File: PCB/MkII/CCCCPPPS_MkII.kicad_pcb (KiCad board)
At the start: 2 copper layers, 58 x 20 mm, 30 parts, among them J1 PROG_HEADER, J2 USB_C, J3 CONN_OUT, J4 CONN_IN, Q1 AO3400A, U2 CH32V003AxMx, U3 AP2112K-3.3

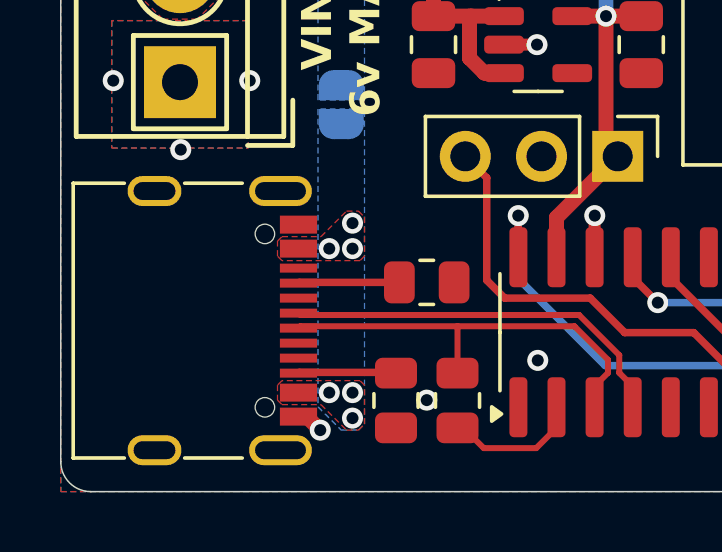
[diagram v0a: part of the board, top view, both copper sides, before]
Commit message: Fixed MkII USB and Polarity issues. MkIIB
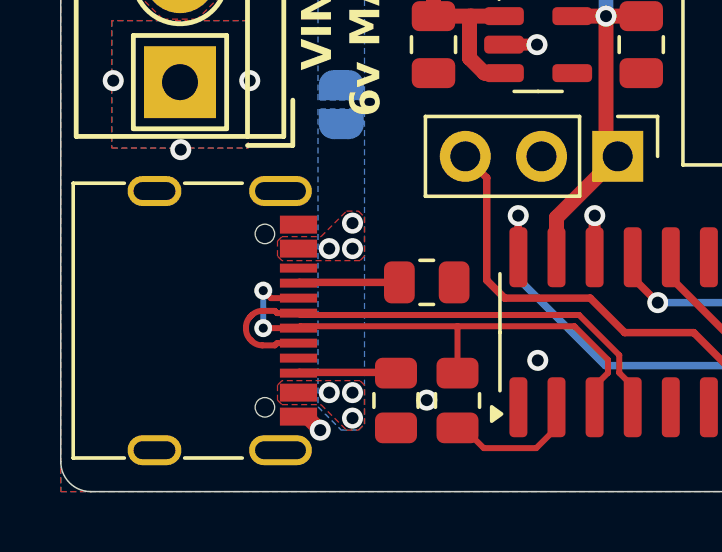
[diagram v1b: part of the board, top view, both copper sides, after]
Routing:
- net /USB_DP: track 13.2 -> 17.4 mm
- net /USB_DN: track 14.1 -> 17.8 mm, vias 0 -> 2
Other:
- board text added: "+"
- board text added: "-"
- board text added: "2024 MkIIB ADBeta Bogdan Ionescu"
- board text added: "3V3"
- board text removed: "2024 MkII ADBeta Bogdan Ionescu"
- board text removed: "3v3"
